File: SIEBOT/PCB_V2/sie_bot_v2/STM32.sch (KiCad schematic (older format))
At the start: 49 parts, among them P6 CONN_5X2, P8 CONN_12X2, P9 CONN_12X2, Q2 BS170F, Q3 BS170F, Q4 BS170F, Q5 BS170F, Q6 BS170F, Q7 BS170F, Q8 BS170F, Q9 BS170F, U10 STM32F105RC, U11 LT1117CST-3.3, U12 ZXMHC3F381N8, U13 ZXMHC3F381N8, U14 ZXMHC3F381N8, U15 ZXMHC3F381N8, X3 12MHz

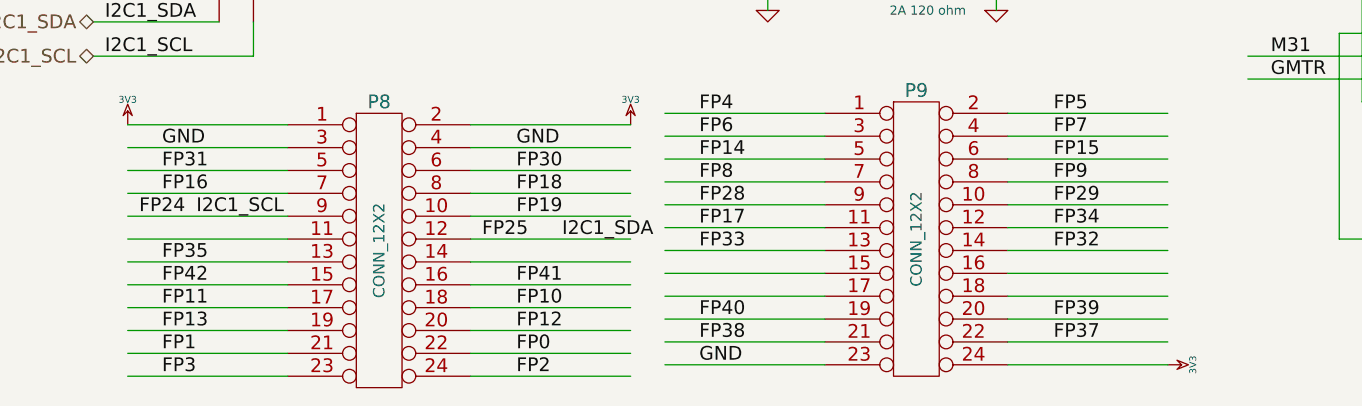
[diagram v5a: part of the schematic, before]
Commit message: Ruteo de las señales de alimentación.
TODO:
agregar footprints en los pines 47 y 31 del STM32 para compatibilidad con el stm32f4

Colocar etiquetas en los pines de los conectores del STM32
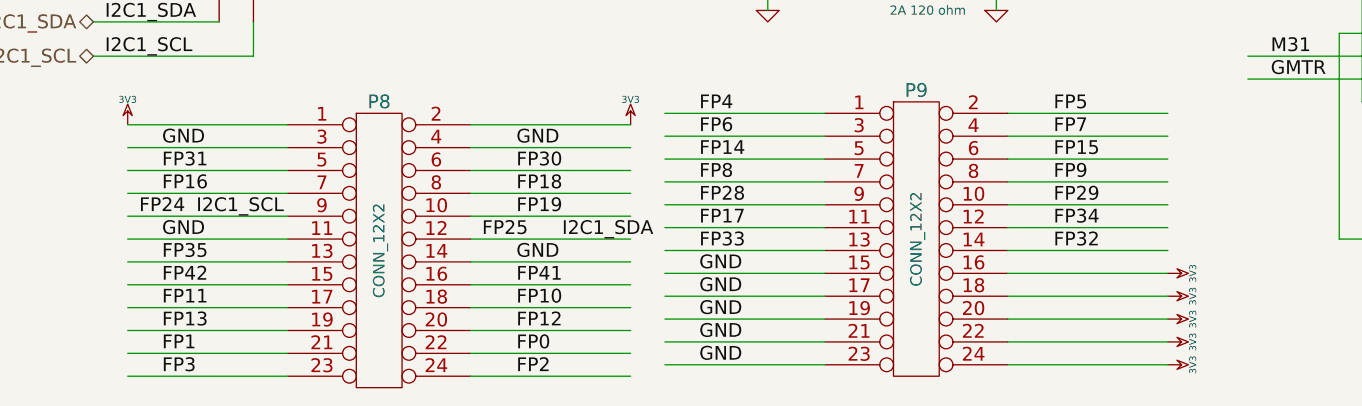
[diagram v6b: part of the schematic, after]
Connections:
- net labels removed: FP37, FP38, FP39, FP40
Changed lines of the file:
@@
-EESchema Schematic File Version 2  date Thu 16 Feb 2012 10:36:53 AM COT
+EESchema Schematic File Version 2  date Fri 17 Feb 2012 09:28:31 AM COT
 LIBS:con-jack
 LIBS:adm3101e
@@
 Sheet 3 5
 Title ""
-Date "16 feb 2012"
+Date "17 feb 2012"
 Rev ""
 Comp ""
@@
 Comment4 ""
 $EndDescr
+$Comp
+L 3V3 #PWR89
+U 1 1 4F3E63FA
+P 6050 8850
+F 0 "#PWR89" H 6050 8950 30  0001 C CNN
+F 1 "3V3" H 6050 8960 30  0000 C CNN
+	1    6050 8850
+	0    1    1    0
+$EndComp
+$Comp
+L 3V3 #PWR88
+U 1 1 4F3E63F9
+P 6050 8750
+F 0 "#PWR88" H 6050 8850 30  0001 C CNN
+F 1 "3V3" H 6050 8860 30  0000 C CNN
+	1    6050 8750
+	0    1    1    0
+$EndComp
+Text Label 4000 8850 0    60   ~ 0
+GND
+Text Label 4000 8750 0    60   ~ 0
+GND
+Text Label 1650 8400 0    60   ~ 0
+GND
+Text Label 3200 8500 0    60   ~ 0
+GND
+$Comp
+L 3V3 #PWR86
+U 1 1 4F3E4E25
+P 6050 8550
+F 0 "#PWR86" H 6050 8650 30  0001 C CNN
+F 1 "3V3" H 6050 8660 30  0000 C CNN
+	1    6050 8550
+	0    1    1    0
+$EndComp
+$Comp
+L 3V3 #PWR87
+U 1 1 4F3E4E22
+P 6050 8650
+F 0 "#PWR87" H 6050 8750 30  0001 C CNN
+F 1 "3V3" H 6050 8760 30  0000 C CNN
+	1    6050 8650
+	0    1    1    0
+$EndComp
+Text Label 4000 8650 0    60   ~ 0
+GND
+Text Label 4000 8550 0    60   ~ 0
+GND
 Text Label 5950 4500 0    60   ~ 0
 C2M4
@@
 I2C1_SDA
 $Comp
-L 3V3 #PWR86
+L 3V3 #PWR90
 U 1 1 4E8A099D
 P 6050 8950
-F 0 "#PWR86" H 6050 9050 30  0001 C CNN
+F 0 "#PWR90" H 6050 9050 30  0001 C CNN
 F 1 "3V3" H 6050 9060 30  0000 C CNN
 	1    6050 8950
@@
 	1    0    0    -1
 $EndComp
-Text Label 5550 8850 0    60   ~ 0
-FP37
-Text Label 5550 8750 0    60   ~ 0
-FP39
-Text Label 4000 8850 0    60   ~ 0
-FP38
 Text Label 5550 7850 0    60   ~ 0
 FP5
@@
 Text Label 4000 8450 0    60   ~ 0
 FP33
-Text Label 4000 8750 0    60   ~ 0
-FP40
 Text Label 4000 7850 0    60   ~ 0
 FP4
@@
 $EndComp
 $Comp
-L 3V3 #PWR91
+L 3V3 #PWR95
 U 1 1 4E7B4482
 P 8150 900
-F 0 "#PWR91" H 8150 1000 30  0001 C CNN
+F 0 "#PWR95" H 8150 1000 30  0001 C CNN
 F 1 "3V3" H 8150 1010 30  0000 C CNN
 	1    8150 900
@@
 $EndComp
 $Comp
-L 3V3 #PWR94
+L 3V3 #PWR98
 U 1 1 4E78C319
 P 8550 2150
-F 0 "#PWR94" H 8550 2250 30  0001 C CNN
+F 0 "#PWR98" H 8550 2250 30  0001 C CNN
 F 1 "3V3" H 8550 2260 30  0000 C CNN
 	1    8550 2150
@@
 $EndComp
 $Comp
-L 3V3 #PWR93
+L 3V3 #PWR97
 U 1 1 4E2A2E11
 P 8350 2150
-F 0 "#PWR93" H 8350 2250 30  0001 C CNN
+F 0 "#PWR97" H 8350 2250 30  0001 C CNN
 F 1 "3V3" H 8350 2260 30  0000 C CNN
 	1    8350 2150
@@
 $EndComp
 $Comp
-L 3V3 #PWR96
+L 3V3 #PWR100
 U 1 1 4E2A2E03
 P 8750 1000
-F 0 "#PWR96" H 8750 1100 30  0001 C CNN
+F 0 "#PWR100" H 8750 1100 30  0001 C CNN
 F 1 "3V3" H 8750 1110 30  0000 C CNN
 	1    8750 1000

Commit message: Adicion de componentes en los pines 47 y 31 (resistencias de 0 Ohms para M3 condensadores de 2.2uF para M4) para permitir el cambio entre el cortex M3 y M4
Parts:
- added C19, C21: 2.2uF, SM0805, symbol C
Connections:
- wire segments 259 -> 252
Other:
- note added: "C19, C21 2.2uF para cortex M4\nC19. C21 = Ohms para cortex M3"
